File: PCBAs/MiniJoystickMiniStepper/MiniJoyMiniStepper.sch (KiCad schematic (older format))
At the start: 71 parts, among them J0 STEPPER_UNI_5P, J1 STEPPER_UNI_5P, J10 TH_0.1_1x1, J100 TH_0.1_1x1, J101 TH_0.1_1x1, J102 TH_0.1_1x1, J103 TH_0.1_1x1, J104 TH_0.1_1x1, J105 TH_0.1_1x1, J107 TH_0.1_1x1, J11 TH_0.1_1x1, J12 TH_0.1_1x1, J13 TH_0.1_1x1, J14 TH_0.1_1x1, J15 TH_0.1_1x1, J16 TH_0.1_1x1, J2 STEPPER_UNI_5P, J3 STEPPER_UNI_5P, J4 STEPPER_UNI_5P, J5 STEPPER_UNI_5P, J6 STEPPER_UNI_5P, J7 STEPPER_UNI_5P, J8 TH_0.1_1x1, J9 TH_0.1_1x1, U1 MCP3008T-I/SL, U10 ULN2803, U11 STM32F103C8T6_BLUE_PILL, U2 OLED_128x32_I2C, U3 CD74HC595, U4 CD74HC595, U5 CD74HC595, U6 CD74HC595, U7 ULN2803, U8 ULN2803, U9 ULN2803

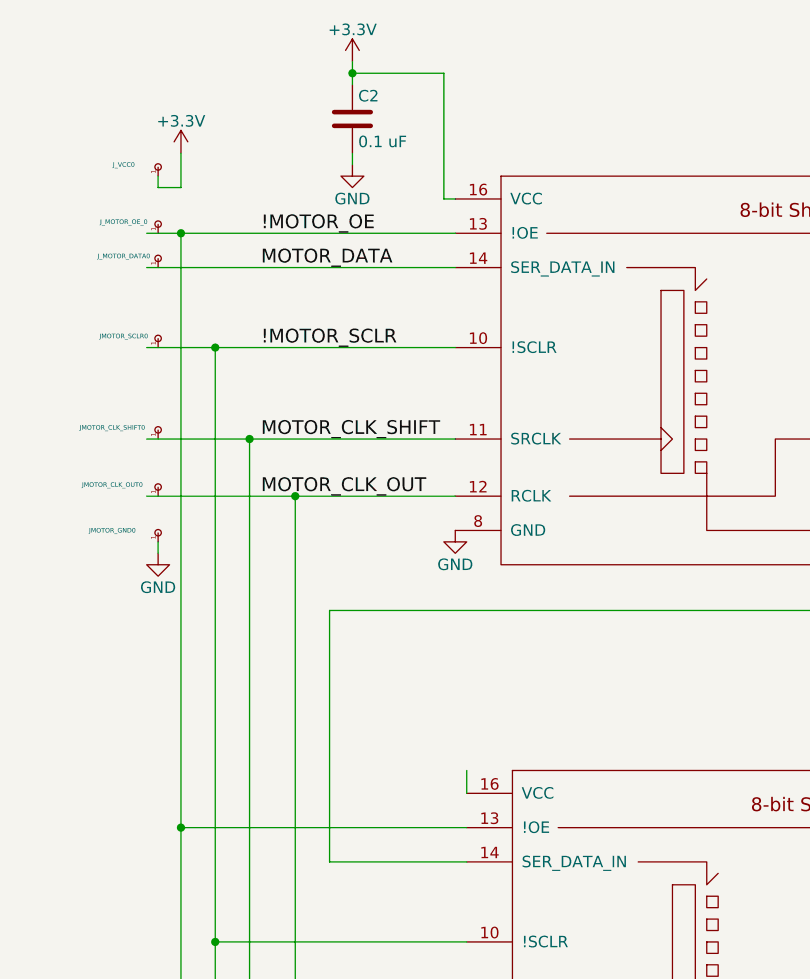
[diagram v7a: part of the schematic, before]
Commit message: Fixed cut/paste instead of copy/paste bug
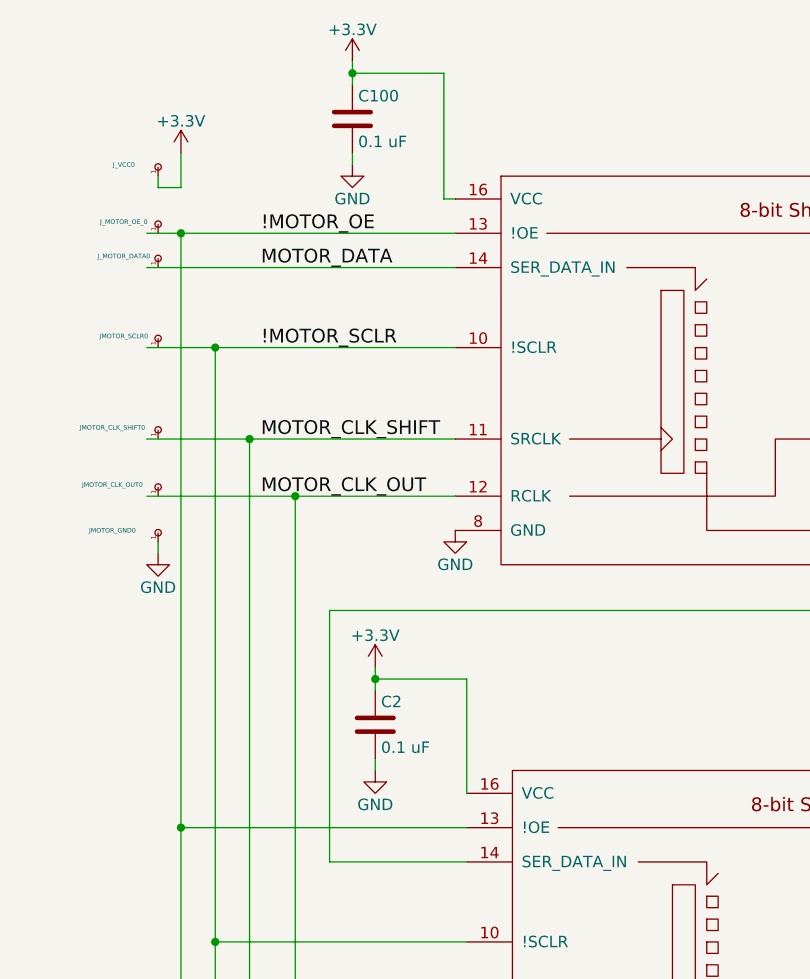
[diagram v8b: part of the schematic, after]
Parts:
- added C2: 0.1 uF, Capacitors_SMD:C_0603, symbol C
- renumbered C2 to C100
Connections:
- wire segments 413 -> 416
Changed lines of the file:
@@
 Connection ~ 15400 4900
 Wire Wire Line
-	16350 3850 16350 3750
+	16350 3350 16350 3850
 Wire Wire Line
 	1650 9050 1800 9050
@@
 	15000 2750 15000 2800
 $Comp
-L C C2
+L C C100
 U 1 1 5A931243
 P 15850 900
-F 0 "C2" H 15875 1000 50  0000 L CNN
+F 0 "C100" H 15875 1000 50  0000 L CNN
 F 1 "0.1 uF" H 15875 800 50  0000 L CNN
 F 2 "Capacitors_SMD:C_0603" H 15888 750 50  0001 C CNN
@@
 Wire Wire Line
 	16250 700  15850 700
+$Comp
+L C C2
+U 1 1 5A93B88B
+P 15950 3550
+F 0 "C2" H 15975 3650 50  0000 L CNN
+F 1 "0.1 uF" H 15975 3450 50  0000 L CNN
+F 2 "Capacitors_SMD:C_0603" H 15988 3400 50  0001 C CNN
+F 3 "" H 15950 3550 50  0000 C CNN
+F 4 "YAEGO" H 15950 3550 60  0001 C CNN "MFG"
+F 5 "CC0603KRX7R9BB104" H 15950 3550 60  0001 C CNN "MPN"
+	1    15950 3550
+	1    0    0    -1
+$EndComp
+$Comp
+L +3.3V #PWR?
+U 1 1 5A93B891
+P 15950 3300
+F 0 "#PWR?" H 15950 3150 50  0001 C CNN
+F 1 "+3.3V" H 15950 3440 50  0000 C CNN
+F 2 "" H 15950 3300 50  0000 C CNN
+F 3 "" H 15950 3300 50  0000 C CNN
+	1    15950 3300
+	1    0    0    -1
+$EndComp
+$Comp
+L GND #PWR?
+U 1 1 5A93B897
+P 15950 3750
+F 0 "#PWR?" H 15950 3500 50  0001 C CNN
+F 1 "GND" H 15950 3600 50  0000 C CNN
+F 2 "" H 15950 3750 50  0000 C CNN
+F 3 "" H 15950 3750 50  0000 C CNN
+	1    15950 3750
+	1    0    0    -1
+$EndComp
+Wire Wire Line
+	15950 3300 15950 3400
+Wire Wire Line
+	15950 3700 15950 3750
+Connection ~ 15950 3350
+Wire Wire Line
+	16350 3350 15950 3350
 $EndSCHEMATC
